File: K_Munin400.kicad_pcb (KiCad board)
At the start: 2 copper layers, 1 part

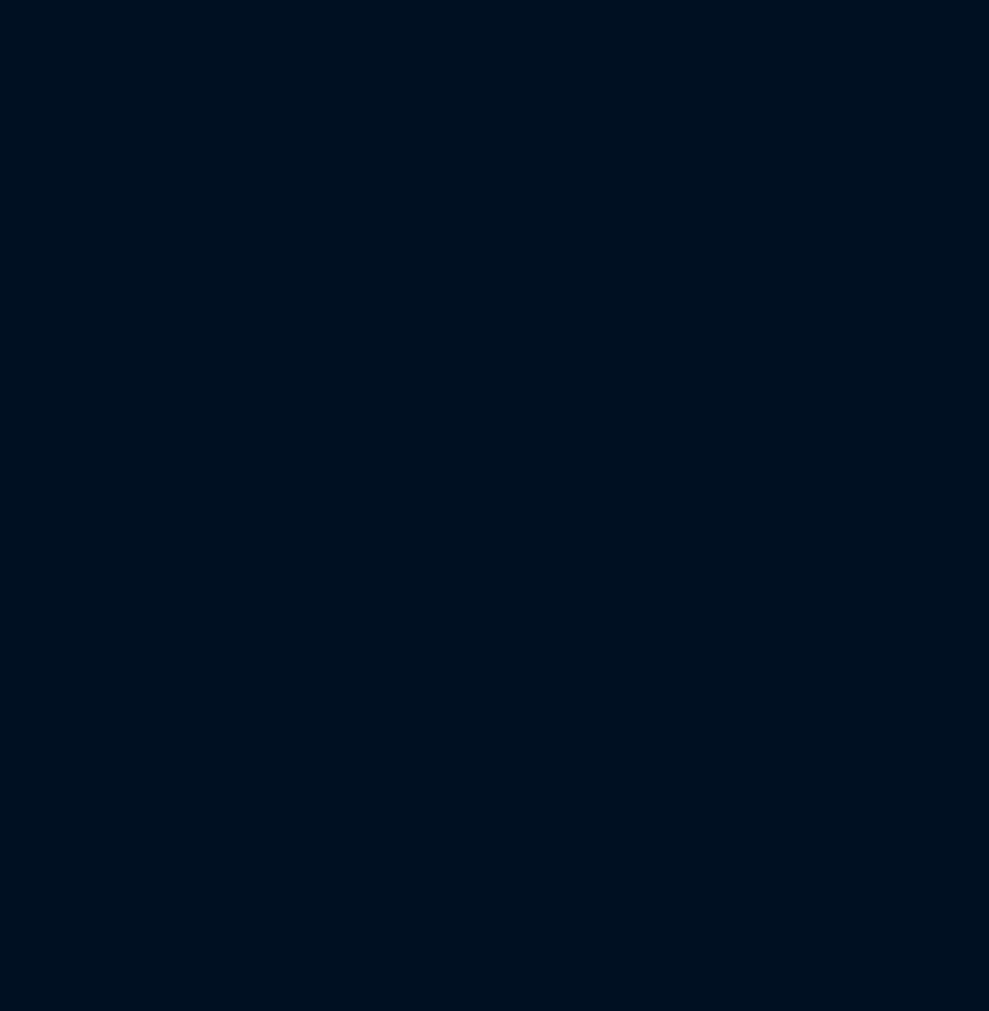
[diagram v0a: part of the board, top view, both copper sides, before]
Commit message: all footprint and 3D module defined, schematic completed
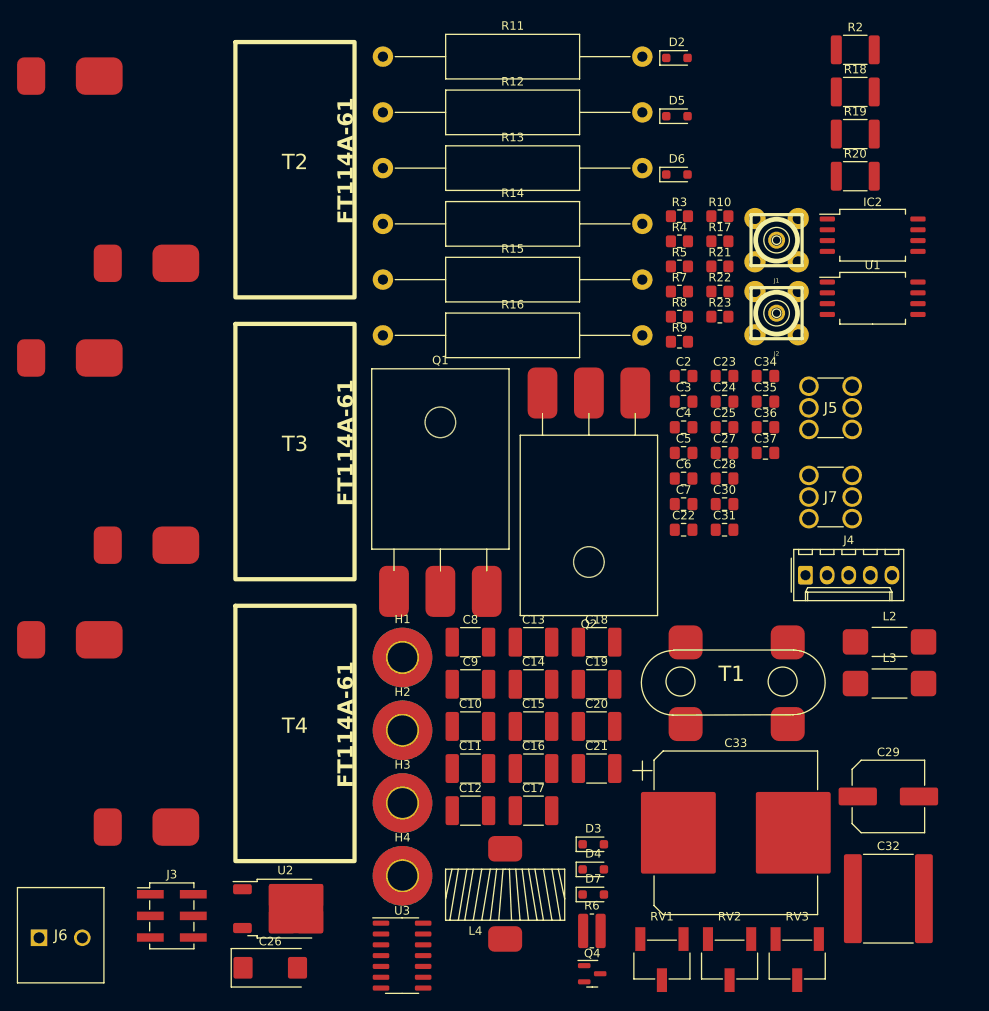
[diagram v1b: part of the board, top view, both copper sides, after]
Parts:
- added C10: 10n/250V, Capacitor_SMD:C_1812_4532Metric_Pad1.57x3.40mm_HandSolder, F.Cu at (54.3, 81.5)
- added C11: 1u/250V, Capacitor_SMD:C_1812_4532Metric_Pad1.57x3.40mm_HandSolder, F.Cu at (54.3, 86.4)
- added C12: TBD, Capacitor_SMD:C_1812_4532Metric_Pad1.57x3.40mm_HandSolder, F.Cu at (54.3, 91.4)
- added C13: TBD, Capacitor_SMD:C_1812_4532Metric_Pad1.57x3.40mm_HandSolder, F.Cu at (61.7, 71.6)
- added C14: 100n, Capacitor_SMD:C_1812_4532Metric_Pad1.57x3.40mm_HandSolder, F.Cu at (61.7, 76.5)
- added C15: 100n, Capacitor_SMD:C_1812_4532Metric_Pad1.57x3.40mm_HandSolder, F.Cu at (61.7, 81.5)
- added C16: 100n, Capacitor_SMD:C_1812_4532Metric_Pad1.57x3.40mm_HandSolder, F.Cu at (61.7, 86.4)
- added C17: 100n, Capacitor_SMD:C_1812_4532Metric_Pad1.57x3.40mm_HandSolder, F.Cu at (61.7, 91.4)
- added C18: 100n, Capacitor_SMD:C_1812_4532Metric_Pad1.57x3.40mm_HandSolder, F.Cu at (69.1, 71.6)
- added C19: 100n, Capacitor_SMD:C_1812_4532Metric_Pad1.57x3.40mm_HandSolder, F.Cu at (69.1, 76.5)
- added C2: 10n, Capacitor_SMD:C_0805_2012Metric_Pad1.18x1.45mm_HandSolder, F.Cu at (79.3, 40.3)
- added C20: 100n, Capacitor_SMD:C_1812_4532Metric_Pad1.57x3.40mm_HandSolder, F.Cu at (69.1, 81.5)
- added C21: 100n, Capacitor_SMD:C_1812_4532Metric_Pad1.57x3.40mm_HandSolder, F.Cu at (69.1, 86.4)
- added C22: 100n, Capacitor_SMD:C_0805_2012Metric_Pad1.18x1.45mm_HandSolder, F.Cu at (79.3, 58.4)
- added C23: 1u, Capacitor_SMD:C_0805_2012Metric_Pad1.18x1.45mm_HandSolder, F.Cu at (84.1, 40.3)
- added C24: 1u, Capacitor_SMD:C_0805_2012Metric_Pad1.18x1.45mm_HandSolder, F.Cu at (84.1, 43.3)
- added C25: 1u, Capacitor_SMD:C_0805_2012Metric_Pad1.18x1.45mm_HandSolder, F.Cu at (84.1, 46.3)
- added C26: 10u, Capacitor_Tantalum_SMD:CP_EIA-7343-31_Kemet-D_Pad2.25x2.55mm_HandSolder, F.Cu at (30.8, 109.8)
- added C27: 100n, Capacitor_SMD:C_0805_2012Metric_Pad1.18x1.45mm_HandSolder, F.Cu at (84.1, 49.3)
- added C28: 100n, Capacitor_SMD:C_0805_2012Metric_Pad1.18x1.45mm_HandSolder, F.Cu at (84.1, 52.3)
- added C29: 220u, Capacitor_SMD:C_Elec_8x10.2, F.Cu at (103.4, 89.7)
- added C3: 10n, Capacitor_SMD:C_0805_2012Metric_Pad1.18x1.45mm_HandSolder, F.Cu at (79.3, 43.3)
- added C30: 10n, Capacitor_SMD:C_0805_2012Metric_Pad1.18x1.45mm_HandSolder, F.Cu at (84.1, 55.4)
- added C31: 1u, Capacitor_SMD:C_0805_2012Metric_Pad1.18x1.45mm_HandSolder, F.Cu at (84.1, 58.4)
- added C32: 22u/63V, Capacitor_SMD:C_3640_9110Metric_Pad2.10x10.45mm_HandSolder, F.Cu at (103.4, 101.7)
- added C33: 330u/63V, Capacitor_SMD:CP_Elec_18x17.5, F.Cu at (85.5, 94.0)
- added C34: 1u, Capacitor_SMD:C_0805_2012Metric_Pad1.18x1.45mm_HandSolder, F.Cu at (88.9, 40.3)
- added C35: 100n, Capacitor_SMD:C_0805_2012Metric_Pad1.18x1.45mm_HandSolder, F.Cu at (88.9, 43.3)
- added C36: 1n, Capacitor_SMD:C_0805_2012Metric_Pad1.18x1.45mm_HandSolder, F.Cu at (88.9, 46.3)
- added C37: 1u, Capacitor_SMD:C_0805_2012Metric_Pad1.18x1.45mm_HandSolder, F.Cu at (88.9, 49.3)
- added C4: 100n, Capacitor_SMD:C_0805_2012Metric_Pad1.18x1.45mm_HandSolder, F.Cu at (79.3, 46.3)
- added C5: 100n, Capacitor_SMD:C_0805_2012Metric_Pad1.18x1.45mm_HandSolder, F.Cu at (79.3, 49.3)
- added C6: 1u, Capacitor_SMD:C_0805_2012Metric_Pad1.18x1.45mm_HandSolder, F.Cu at (79.3, 52.3)
- added C7: 100n, Capacitor_SMD:C_0805_2012Metric_Pad1.18x1.45mm_HandSolder, F.Cu at (79.3, 55.4)
- added C8: 1u/250V, Capacitor_SMD:C_1812_4532Metric_Pad1.57x3.40mm_HandSolder, F.Cu at (54.3, 71.6)
- added C9: 10n/250V, Capacitor_SMD:C_1812_4532Metric_Pad1.57x3.40mm_HandSolder, F.Cu at (54.3, 76.5)
- added D2: CDSOD323-TC15, Diode_SMD:D_SOD-323_HandSoldering, F.Cu at (78.5, 2.92)
- added D3: BAS16J, Diode_SMD:D_SOD-323_HandSoldering, F.Cu at (68.7, 95.3)
- added D4: BAS16J, Diode_SMD:D_SOD-323_HandSoldering, F.Cu at (68.7, 98.3)
- added D5: CDSOD323-TC03, Diode_SMD:D_SOD-323_HandSoldering, F.Cu at (78.5, 9.78)
- added D6: CDSOD323-TC03, Diode_SMD:D_SOD-323_HandSoldering, F.Cu at (78.5, 16.6)
- added D7: BAS16J, Diode_SMD:D_SOD-323_HandSoldering, F.Cu at (68.7, 101.2)
- added H1: MountingHole_Pad, MountingHole:MountingHole_3.5mm_Pad_TopBottom, F.Cu at (46.3, 73.4)
- added H2: MountingHole_Pad, MountingHole:MountingHole_3.5mm_Pad_TopBottom, F.Cu at (46.3, 81.9)
- added H3: MountingHole_Pad, MountingHole:MountingHole_3.5mm_Pad_TopBottom, F.Cu at (46.3, 90.5)
- added H4: MountingHole_Pad, MountingHole:MountingHole_3.5mm_Pad_TopBottom, F.Cu at (46.3, 99.0)
- added IC2: ACHS-7123-000E, Package_SO:SOIC-8_7.5x5.85mm_P1.27mm, F.Cu at (101.5, 23.8)
- added J1: Conn_Coaxial, SMA_PINS:SMA_PINS, F.Cu at (90.2, 24.3)
- added J2: Conn_Coaxial, SMA_PINS:SMA_PINS, F.Cu at (90.2, 32.9)
- added J3: Conn_02x03_Odd_Even, Connector_PinHeader_2.54mm:PinHeader_2x03_P2.54mm_Vertical_SMD, F.Cu at (19.2, 103.7)
- added J4: To P.A., Connector_Molex:Molex_KK-254_AE-6410-05A_1x05_P2.54mm_Vertical, F.Cu at (93.6, 63.7)
- added J5: Wurth Redcube 7461057, 7461057:7461057, F.Cu at (94.0, 41.5)
- added J6: Phoenix/1711725, 1711725:1711725, F.Cu at (3.59, 106.3)
- added J7: Wurth Redcube 7461057, 7461057:7461057, F.Cu at (94.0, 52.0)
- added L2: 2743021447, Fair-Rite_2743021447:Fair-Rite_2743021447, F.Cu at (103.5, 71.5)
- added L3: 2743021447, Fair-Rite_2743021447:Fair-Rite_2743021447, F.Cu at (103.5, 76.4)
- added L4: FT82-61?, T50:T50_V_smd, F.Cu at (58.4, 101.2)
- added Q1: MRF300AN tab dwn, MRF300AN:TO-247-3_Horizontal_TabDown, F.Cu at (45.3, 65.6)
- added Q2: MRF300BN tab up, MRF300BN:TO-247-3_Horizontal_TabUp, F.Cu at (62.7, 42.3)
- added Q4: BSS84, Package_TO_SOT_SMD:SOT-23, F.Cu at (68.6, 110.5)
- added R10: 1R, Resistor_SMD:R_0805_2012Metric_Pad1.20x1.40mm_HandSolder, F.Cu at (83.6, 21.5)
- added R11: 470R, Resistor_THT:R_Axial_DIN0516_L15.5mm_D5.0mm_P30.48mm_Horizontal, F.Cu at (44.0, 2.77)
- added R12: 470R, Resistor_THT:R_Axial_DIN0516_L15.5mm_D5.0mm_P30.48mm_Horizontal, F.Cu at (44.0, 9.32)
- added R13: 470R, Resistor_THT:R_Axial_DIN0516_L15.5mm_D5.0mm_P30.48mm_Horizontal, F.Cu at (44.0, 15.9)
- added R14: 470R, Resistor_THT:R_Axial_DIN0516_L15.5mm_D5.0mm_P30.48mm_Horizontal, F.Cu at (44.0, 22.4)
- added R15: 470R, Resistor_THT:R_Axial_DIN0516_L15.5mm_D5.0mm_P30.48mm_Horizontal, F.Cu at (44.0, 29.0)
- added R16: 470R, Resistor_THT:R_Axial_DIN0516_L15.5mm_D5.0mm_P30.48mm_Horizontal, F.Cu at (44.0, 35.5)
- added R17: 10k, Resistor_SMD:R_0805_2012Metric_Pad1.20x1.40mm_HandSolder, F.Cu at (83.6, 24.5)
- added R18: 4R7, Resistor_SMD:R_1812_4532Metric_Pad1.30x3.40mm_HandSolder, F.Cu at (99.5, 6.92)
- added R19: 4R7, Resistor_SMD:R_1812_4532Metric_Pad1.30x3.40mm_HandSolder, F.Cu at (99.5, 11.9)
- added R2: 5R6, Resistor_SMD:R_1812_4532Metric_Pad1.30x3.40mm_HandSolder, F.Cu at (99.5, 1.98)
- added R20: 4R7, Resistor_SMD:R_1812_4532Metric_Pad1.30x3.40mm_HandSolder, F.Cu at (99.5, 16.8)
- added R21: 27k, Resistor_SMD:R_0805_2012Metric_Pad1.20x1.40mm_HandSolder, F.Cu at (83.6, 27.4)
- added R22: 10k, Resistor_SMD:R_0805_2012Metric_Pad1.20x1.40mm_HandSolder, F.Cu at (83.6, 30.4)
- added R23: 100R, Resistor_SMD:R_0805_2012Metric_Pad1.20x1.40mm_HandSolder, F.Cu at (83.6, 33.3)
- added R3: 22R, Resistor_SMD:R_0805_2012Metric_Pad1.20x1.40mm_HandSolder, F.Cu at (78.8, 21.5)
- added R4: 220R, Resistor_SMD:R_0805_2012Metric_Pad1.20x1.40mm_HandSolder, F.Cu at (78.8, 24.5)
- added R5: NTC10K, Resistor_SMD:R_0805_2012Metric_Pad1.20x1.40mm_HandSolder, F.Cu at (78.8, 27.4)
- added R6: 1.2k, Resistor_SMD:R_0815_2038Metric_Pad1.20x4.05mm_HandSolder, F.Cu at (68.5, 105.5)
- added R7: 220R, Resistor_SMD:R_0805_2012Metric_Pad1.20x1.40mm_HandSolder, F.Cu at (78.8, 30.4)
- added R8: 22R, Resistor_SMD:R_0805_2012Metric_Pad1.20x1.40mm_HandSolder, F.Cu at (78.8, 33.3)
- added R9: 1R, Resistor_SMD:R_0805_2012Metric_Pad1.20x1.40mm_HandSolder, F.Cu at (78.8, 36.3)
- added RV1: 10k, Potentiometer_SMD:Potentiometer_Bourns_3269W_Vertical, F.Cu at (76.8, 108.9)
- added RV2: 10k, Potentiometer_SMD:Potentiometer_Bourns_3269W_Vertical, F.Cu at (84.7, 108.9)
- added RV3: 1k, Potentiometer_SMD:Potentiometer_Bourns_3269W_Vertical, F.Cu at (92.7, 108.9)
- added T1: BN43-202 3:1, BN43-202-master:BN43-202, F.Cu at (85.0, 76.2)
- added T2: FT-114A-61, FT114A:FT114A-61, F.Cu at (33.7, 16.1)
- added T3: FT-114A-61, FT114A:FT114A-61, F.Cu at (33.7, 49.2)
- added T4: FT-114A-61, FT114A:FT114A-61, F.Cu at (33.7, 82.3)
- added U1: LM358, Package_SO:SOIC-8_7.5x5.85mm_P1.27mm, F.Cu at (101.5, 31.2)
- added U2: LM78M05_TO252, Package_TO_SOT_SMD:TO-252-2, F.Cu at (32.5, 102.9)
- added U3: LMC660AIM_NOPB, Package_SO:SOIC-14_3.9x8.7mm_P1.27mm, F.Cu at (46.2, 108.4)

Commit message: 3Dshapes set
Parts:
- IC2, U1: footprint Package_SO:SOIC-8_7.5x5.85mm_P1.27mm -> Package_SO:SOIC-8_3.9x4.9mm_P1.27mm
- R6: footprint Resistor_SMD:R_0815_2038Metric_Pad1.20x4.05mm_HandSolder -> Resistor_SMD:R_0805_2012Metric_Pad1.20x1.40mm_HandSolder
- moved G*** 65.1 mm to (113.8, 50.9)

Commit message: some debuging, new placement, silk logo
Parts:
- added H5: MountingHole_Pad, MountingHole:MountingHole_3.5mm_Pad_TopBottom, F.Cu at (79.0, 106.0)
- added REF**: KiCad-Logo2_5mm_SilkScreen, Symbol:KiCad-Logo2_5mm_SilkScreen, F.Cu at (148.0, 70.0)
- added REF**: OSHW-Logo2_9.8x8mm_SilkScreen, Symbol:OSHW-Logo2_9.8x8mm_SilkScreen, F.Cu at (56.5, 76.0)
- C32: footprint Capacitor_SMD:C_3640_9110Metric_Pad2.10x10.45mm_HandSolder -> Capacitor_SMD:C_2220_5650Metric_Pad1.97x5.40mm_HandSolder
- R5: footprint Resistor_SMD:R_0805_2012Metric_Pad1.20x1.40mm_HandSolder -> Resistor_SMD:R_MELF_MMB-0207
- T3: footprint FT114A:FT114A-61 -> FT114A:FT114A-61_B
- T4: footprint FT114A:FT114A-61 -> FT114A:FT114A-61_out
- moved R11 159.2 mm to (-95.2, 80.0)
- moved C30 154.9 mm to (-53.4, 126.5)
- moved C34 154.9 mm to (-48.6, 111.4)
- moved C35 154.9 mm to (-48.6, 114.5)
- moved C36 154.9 mm to (-48.6, 117.5)
- moved C37 154.9 mm to (-48.6, 120.5)
- moved C6 154.9 mm to (-58.2, 123.5)
- moved J4 154.9 mm to (-43.9, 134.8)
- moved R12 154.9 mm to (-93.6, 80.5)
- moved R13 154.9 mm to (-93.6, 87.0)
- moved R14 154.9 mm to (-93.6, 93.6)
- moved R15 154.9 mm to (-93.6, 100.1)
- moved R16 154.9 mm to (-93.6, 106.7)
- moved R21 154.9 mm to (-54.0, 98.6)
- moved R22 154.9 mm to (-54.0, 101.5)
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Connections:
- C10 pad 2: Net-(D5-A2) -> Net-(C10-Pad2)
- C11 pad 2: Net-(D5-A2) -> Net-(C10-Pad2)
- C20 pad 1: Net-(T3-SA) -> Net-(T3-AB)
- C21 pad 1: Net-(T3-SA) -> Net-(T3-AB)
- C8 pad 2: Net-(D6-A1) -> Net-(C8-Pad2)
- C9 pad 2: Net-(D6-A1) -> Net-(C8-Pad2)
- Q1 pad 1: Net-(Q1-G) -> Net-(D5-A2)
- Q2 pad 1: Net-(Q2-G) -> Net-(D6-A1)
- R10 pad 2: Net-(Q2-G) -> Net-(D6-A1)
- R11 pad 1: Net-(Q2-G) -> Net-(D6-A1)
- R11 pad 2: Net-(D6-A1) -> Net-(C8-Pad2)
- R12 pad 1: Net-(Q2-G) -> Net-(D6-A1)
- R12 pad 2: Net-(D6-A1) -> Net-(C8-Pad2)
- R13 pad 1: Net-(Q2-G) -> Net-(D6-A1)
- R13 pad 2: Net-(D6-A1) -> Net-(C8-Pad2)
- R14 pad 1: Net-(Q1-G) -> Net-(D5-A2)
- R14 pad 2: Net-(D5-A2) -> Net-(C10-Pad2)
- R15 pad 1: Net-(Q1-G) -> Net-(D5-A2)
- R15 pad 2: Net-(D5-A2) -> Net-(C10-Pad2)
- R16 pad 1: Net-(Q1-G) -> Net-(D5-A2)
- R16 pad 2: Net-(D5-A2) -> Net-(C10-Pad2)
- R9 pad 2: Net-(Q1-G) -> Net-(D5-A2)
- T2 pad 1: Net-(Q1-D) -> Net-(Q2-D)
- T2 pad 3: Net-(T2-SA) -> Net-(Q1-D)
- T2 pad 4: Net-(Q2-D) -> Net-(T2-SA)
- T3 pad 2: Net-(T2-SA) -> Net-(T3-AB)
- T3 pad 3: Net-(T3-SA) -> Net-(Q2-D)
- T3 pad 4: Net-(Q2-D) -> Net-(T2-SA)
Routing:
- net +48V: track 0.00 -> 69.4 mm
- net Net-(T2-SA): track 0.00 -> 63.9 mm
- net Net-(T4-AA): track 0.00 -> 11.6 mm
- net Net-(T4-SB): track 0.00 -> 11.4 mm
- net Net-(T3-AB): track 0.00 -> 10.5 mm
- net Net-(T2-AB): track 0.00 -> 10.5 mm
- net GND: vias 0 -> 62
- added copper zone on B.Cu, net GND
- added copper zone on F.Cu, net GND
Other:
- board outline added: 120 x 110 mm
- board text added: "Munin 400 Rev 2 LA2NI"

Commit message: placement and routing completed
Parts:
- removed R12, R13, R14, R15: 470R, Resistor_THT:R_Axial_DIN0516_L15.5mm_D5.0mm_P30.48mm_Horizontal
- removed the REF** at (56.5, 76.0)
- added REF**: OSHW-Logo2_7.3x6mm_SilkScreen, Symbol:OSHW-Logo2_7.3x6mm_SilkScreen, F.Cu at (60.0, 74.4)
- R11, R16: footprint Resistor_THT:R_Axial_DIN0516_L15.5mm_D5.0mm_P30.48mm_Horizontal -> Resistor_feedB:R_Axial_DIN0414_L11.9mm_D4.5mm_P25.40mm_Horizontal
- moved C34 221.6 mm to (168.2, 157.2), turned to -90 degrees
- moved C35 218.9 mm to (166.0, 157.4), turned to -90 degrees
- moved C36 199.4 mm to (147.8, 151.4), turned to 180 degrees
- moved C37 199.2 mm to (147.8, 153.6), turned to 180 degrees
- moved R22 194.9 mm to (136.6, 142.2), turned to 180 degrees
- moved R21 192.8 mm to (133.6, 143.2), turned to -90 degrees
- moved RV3 187.7 mm to (137.8, 136.8)
- moved R23 187.1 mm to (128.5, 145.8), turned to -90 degrees
- moved R11 167.4 mm to (66.3, 124.0)
- moved R16 161.0 mm to (66.3, 88.0)
- moved J4 137.5 mm to (86.7, 178.0), turned to 180 degrees
- moved C30 132.5 mm to (73.5, 164.5), turned to 90 degrees
- moved C6 120.8 mm to (62.5, 126.0), turned to 90 degrees
- moved C32 29.4 mm to (164.5, 131.5), turned to 90 degrees
- moved U3 19.8 mm to (128.5, 138.3), turned to 180 degrees
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- renumbered C22 to locked, L2 to locked
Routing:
- net 5V: track 0.00 -> 146.2 mm
- net A6: track 0.00 -> 57.9 mm
- net +48V: track 69.4 -> 123.4 mm
- net Net-(T2-SA): track 63.9 -> 109.5 mm
- net Net-(IC2-VOUT): track 0.00 -> 36.9 mm
- net Net-(C5-Pad1): track 0.00 -> 34.8 mm
- net PTT_IN: track 0.00 -> 34.5 mm
- net +12V: track 0.00 -> 33.5 mm
- net Net-(IC2-IP-_1): track 0.00 -> 31.3 mm
- net Net-(D3-K): track 0.00 -> 31.3 mm
- net Net-(D4-A): track 0.00 -> 28.9 mm
- net Net-(Q2-D): track 0.00 -> 27.2 mm
- net Net-(Q1-D): track 0.00 -> 21.9 mm
- net Net-(D6-A1): track 0.00 -> 21.6 mm
- net Net-(D5-A2): track 0.00 -> 21.3 mm
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- added copper zone on B.Cu, net +48V
- added copper zone on F.Cu, net +48V
- added copper zone on F.Cu, net Net-(IC2-IP-_1)
- added copper zone on F.Cu, net Net-(T2-SA)
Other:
- board text added: "++12V"
- board text added: "+48V"
- board text added: "GND"
- board text added: "HF In 5W Max"
- board text added: "HF Out 400W"
- board text added: "LA2NI Munin 400 Rev 2"
- board text removed: "Munin 400 Rev 2 LA2NI"

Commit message: new gerber, small pcb mods
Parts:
- removed J4: To P.A., Connector_Molex:Molex_KK-254_AE-6410-05A_1x05_P2.54mm_Vertical
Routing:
- net GND: track 5.89 -> 26.6 mm, vias 267 -> 277
- net (no net): track 20.7 -> 0.00 mm, vias 11 -> 3

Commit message: kicad 10 update, minor schematic changes
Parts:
- removed REF**: OSHW-Logo2_7.3x6mm_SilkScreen, Symbol:OSHW-Logo2_7.3x6mm_SilkScreen
- removed REF**: KiCad-Logo2_5mm_SilkScreen, Symbol:KiCad-Logo2_5mm_SilkScreen
- added C1: 100n, Capacitor_SMD:C_0805_2012Metric, F.Cu at (61.6, 93.0)
- added C38: 100n, Capacitor_SMD:C_0805_2012Metric, F.Cu at (63.4, 116.2)
- added J4: To P.A., Connector_Molex:Molex_KK-254_AE-6410-05A_1x05_P2.54mm_Vertical, F.Cu at (-59.2, 119.8)
- added R1: 6K8, Resistor_SMD:R_0805_2012Metric_Pad1.20x1.40mm_HandSolder, F.Cu at (68.4, 143.0)
- added R12: 470R, Resistor_feedB:R_Axial_DIN0414_L11.9mm_D4.5mm_P25.40mm_Horizontal, F.Cu at (-59.0, 84.4)
- added R13: 470R, Resistor_feedB:R_Axial_DIN0414_L11.9mm_D4.5mm_P25.40mm_Horizontal, F.Cu at (-59.0, 93.4)
- added R14: 470R, Resistor_feedB:R_Axial_DIN0414_L11.9mm_D4.5mm_P25.40mm_Horizontal, F.Cu at (-59.0, 102.4)
- added R15: 470R, Resistor_feedB:R_Axial_DIN0414_L11.9mm_D4.5mm_P25.40mm_Horizontal, F.Cu at (-59.0, 111.4)
- J3: footprint Connector_PinHeader_2.54mm:PinHeader_2x03_P2.54mm_Vertical_SMD -> Connector_IDC:IDC-Header_2x03_P2.54mm_Vertical_SMD
- T2, T3, T4: value FT-114A-61 -> 5961001201
- moved J2 18.4 mm to (149.0, 80.5)
- moved H4 16.8 mm to (149.0, 70.0)
- moved J7 16.3 mm to (135.9, 162.3)
- moved H2 16.0 mm to (149.0, 165.0)
- moved J5 15.1 mm to (147.3, 148.3)
- moved C34 14.8 mm to (153.4, 157.8)
- moved C35 14.6 mm to (151.4, 157.8)
- moved C32 14.5 mm to (150.0, 132.0)
- moved C33 13.5 mm to (122.1, 157.8)
- moved RV3 13.5 mm to (124.3, 137.2)
- moved C36 13.5 mm to (134.3, 151.8)
- moved C37 13.5 mm to (134.3, 154.0)
- moved R18 13.5 mm to (152.0, 139.2)
- moved R19 13.5 mm to (148.0, 139.2)
- moved R20 13.5 mm to (144.0, 139.2)
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- renumbered locked to C22, locked to L2
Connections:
- R5 pad 1: Net-(C5-Pad1) -> Net-(R1-Pad2)
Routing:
- net +48V: track 123.4 -> 48.9 mm
- net Net-(T2-SA): track 109.5 -> 148.7 mm
- net GND: track 26.6 -> 64.8 mm, vias 277 -> 237
- net 5V: track 146.2 -> 132.4 mm
- net A6: track 57.9 -> 44.6 mm
- net Net-(Q1-D): track 21.9 -> 31.7 mm
- net Net-(C5-Pad1): track 34.8 -> 27.0 mm
- net Net-(T3-AB): track 10.5 -> 18.1 mm
- net Net-(T2-AB): track 10.5 -> 18.1 mm
- net Net-(R1-Pad2): track 0.00 -> 5.68 mm
- net Net-(T4-AA): track 11.6 -> 17.0 mm
- net Net-(T4-SB): track 11.4 -> 16.6 mm
- net Net-(IC2-IP-_1): track 31.3 -> 26.1 mm
- net Net-(C10-Pad2): track 9.49 -> 13.4 mm
- net Net-(Q2-D): track 27.2 -> 30.2 mm
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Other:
- board size 120 x 110 mm -> 105 x 104 mm
